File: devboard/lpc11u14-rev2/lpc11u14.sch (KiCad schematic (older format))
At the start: 26 parts, among them CON1 CORTEX-DEBUGGER, J1 microusb, Q1 Q_NPN_BEC, SW1 SW_Push, SW2 SW_Push, U1 LPC11U14FHN33_201, U2 LM1117-3.3, Y1 8MHz

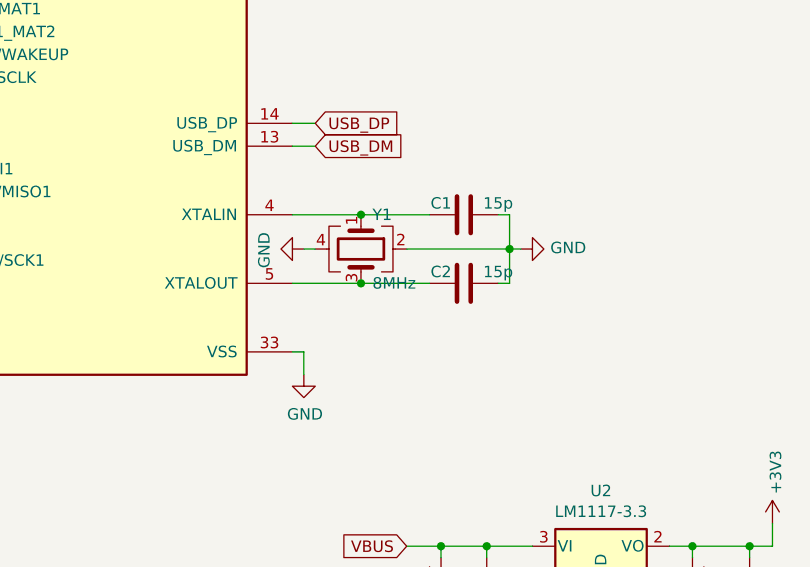
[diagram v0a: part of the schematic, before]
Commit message: default 12MHz
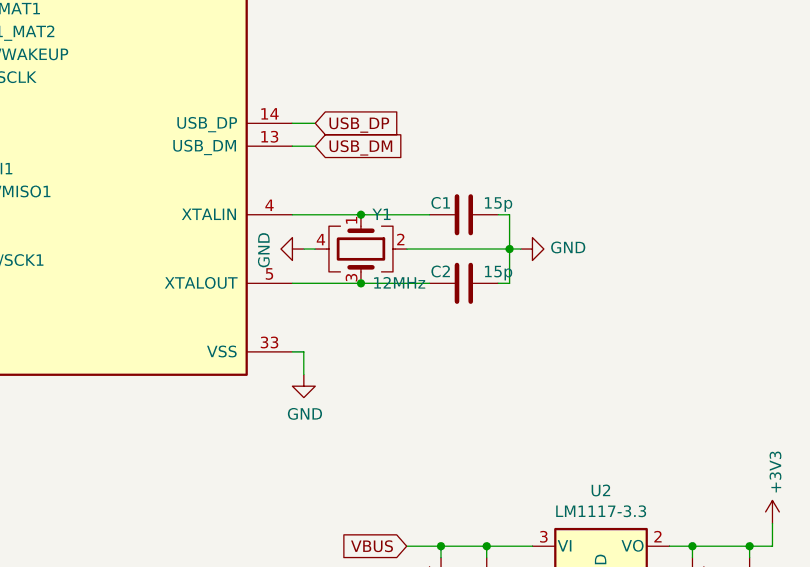
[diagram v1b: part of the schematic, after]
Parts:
- Y1: value 8MHz -> 12MHz
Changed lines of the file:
@@
 P 5300 4150
 F 0 "Y1" V 5150 4200 50  0000 L CNN
-F 1 "8MHz" V 5450 4200 50  0000 L CNN
+F 1 "12MHz" V 5450 4200 50  0000 L CNN
 F 2 "Crystal:Crystal_SMD_3225-4Pin_3.2x2.5mm" H 5300 4150 50  0001 C CNN
 F 3 "~" H 5300 4150 50  0001 C CNN
